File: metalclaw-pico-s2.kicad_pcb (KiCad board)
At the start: 4 copper layers, 21 x 51 mm, 73 parts, among them J1 USB_C_Receptacle_USB2.0_14P, J2 Conn_01x05, J3 Conn_02x05_Odd_Even, J4 Conn_Coaxial, SW1 SW_Push, SW2 SW_Push, U1 ESP32-S2, U2 MX25L3236FM2I-08G-TR, U3 APS6404L-3SQRx-SN, U5 XC6220B331MR, Y1 XRCGB40M000F1S2FR0

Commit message: Update PCB layout
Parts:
- removed D1: D_Schottky, Diode_SMD:D_SOD-323F
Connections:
- A2 pad 36: +3V3 -> unconnected-(A2-3V3-Pad36)
- A2 pad 39: VS -> unconnected-(A2-VSYS-Pad39)
- C1 pad 1: VS -> VBUS
- U5 pad 1: VS -> VBUS
- U5 pad 3: VS -> VBUS

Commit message: Fix non-board edge DRC errors
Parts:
- moved R4 4.64 mm to (158.0, 93.2), turned to 90 degrees
- moved R5 3.55 mm to (158.6, 91.2)
- moved R34 3.20 mm to (157.2, 87.0), turned to 90 degrees
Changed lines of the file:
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@@
 	(footprint "Resistor_SMD:R_0201_0603Metric"
 		(layer "F.Cu")
-		(at 158.86 89.7)
+		(at 157.15 87 90)
 		(descr "Resistor SMD 0201 (0603 Metric), square (rectangular) end terminal, IPC-7351 nominal, (Body size source: https://www.vishay.com/docs/20052/crcw0201e3.pdf), generated with kicad-footprint-generator")
 		(tags "resistor")
 		(property "Reference" "R34"
-			(at 0 -1.05 0)
+			(at 0 -1.05 90)
 			(layer "F.SilkS")
 			(effects
@@
 		)
 		(property "Value" "5.1k"
-			(at 0 1.05 0)
+			(at 0 1.05 90)
 			(layer "F.Fab")
 			(effects
@@
 		)
 		(property "Datasheet" "~"
-			(at 0 0 0)
+			(at 0 0 90)
 			(layer "F.Fab")
 			(hide yes)
@@
 		)
 		(property "Description" "Resistor, US symbol"
-			(at 0 0 0)
+			(at 0 0 90)
 			(layer "F.Fab")
 			(hide yes)
@@
 		)
 		(property "Mouser" "71-CRCW02015K10FEDAT "
-			(at 0 0 0)
+			(at 0 0 90)
 			(unlocked yes)
 			(layer "F.Fab")
@@
 		)
 		(fp_text user "${REFERENCE}"
-			(at 0 -0.68 0)
+			(at 0 -0.68 90)
 			(layer "F.Fab")
 			(effects
@@
 		)
 		(pad "" smd roundrect
-			(at -0.345 0)
+			(at -0.345 0 90)
 			(size 0.318 0.36)
 			(layers "F.Paste")
@@
 		)
 		(pad "" smd roundrect
-			(at 0.345 0)
+			(at 0.345 0 90)
 			(size 0.318 0.36)
 			(layers "F.Paste")
@@
 		)
 		(pad "1" smd roundrect
-			(at -0.32 0)
+			(at -0.32 0 90)
 			(size 0.46 0.4)
 			(layers "F.Cu" "F.Mask")
@@
 		)
 		(pad "2" smd roundrect
-			(at 0.32 0)
+			(at 0.32 0 90)
 			(size 0.46 0.4)
 			(layers "F.Cu" "F.Mask")
@@
 	(footprint "Resistor_SMD:R_0201_0603Metric"
 		(layer "F.Cu")
-		(at 161.09 88.75)
+		(at 158.55 91.23)
 		(descr "Resistor SMD 0201 (0603 Metric), square (rectangular) end terminal, IPC-7351 nominal, (Body size source: https://www.vishay.com/docs/20052/crcw0201e3.pdf), generated with kicad-footprint-generator")
 		(tags "resistor")
@@
 	(footprint "Resistor_SMD:R_0201_0603Metric"
 		(layer "F.Cu")
-		(at 158.67 88.61)
+		(at 158.03 93.21 90)
 		(descr "Resistor SMD 0201 (0603 Metric), square (rectangular) end terminal, IPC-7351 nominal, (Body size source: https://www.vishay.com/docs/20052/crcw0201e3.pdf), generated with kicad-footprint-generator")
 		(tags "resistor")
 		(property "Reference" "R4"
-			(at 0 -1.05 0)
+			(at 0 -1.05 90)
 			(layer "F.SilkS")
 			(effects
@@
 		)
 		(property "Value" "220"
-			(at 0 1.05 0)
+			(at 0 1.05 90)
 			(layer "F.Fab")
 			(effects
@@
 		)
 		(property "Datasheet" "~"
-			(at 0 0 0)
+			(at 0 0 90)
 			(layer "F.Fab")
 			(hide yes)
@@
 		)
 		(property "Description" "Resistor, US symbol"
-			(at 0 0 0)
+			(at 0 0 90)
 			(layer "F.Fab")
 			(hide yes)
@@
 		)
 		(property "Mouser" "603-AC0201FR-13220RL "
-			(at 0 0 0)
+			(at 0 0 90)
 			(unlocked yes)
 			(layer "F.Fab")
@@
 		)
 		(fp_text user "${REFERENCE}"
-			(at 0 -0.68 0)
+			(at 0 -0.68 90)
 			(layer "F.Fab")
 			(effects
@@
 		)
 		(pad "" smd roundrect
-			(at -0.345 0)
+			(at -0.345 0 90)
 			(size 0.318 0.36)
 			(layers "F.Paste")
@@
 		)
 		(pad "" smd roundrect
-			(at 0.345 0)
+			(at 0.345 0 90)
 			(size 0.318 0.36)
 			(layers "F.Paste")
@@
 		)
 		(pad "1" smd roundrect
-			(at -0.32 0)
+			(at -0.32 0 90)
 			(size 0.46 0.4)
 			(layers "F.Cu" "F.Mask")
@@
 		)
 		(pad "2" smd roundrect
-			(at 0.32 0)
+			(at 0.32 0 90)
 			(size 0.46 0.4)
 			(layers "F.Cu" "F.Mask")

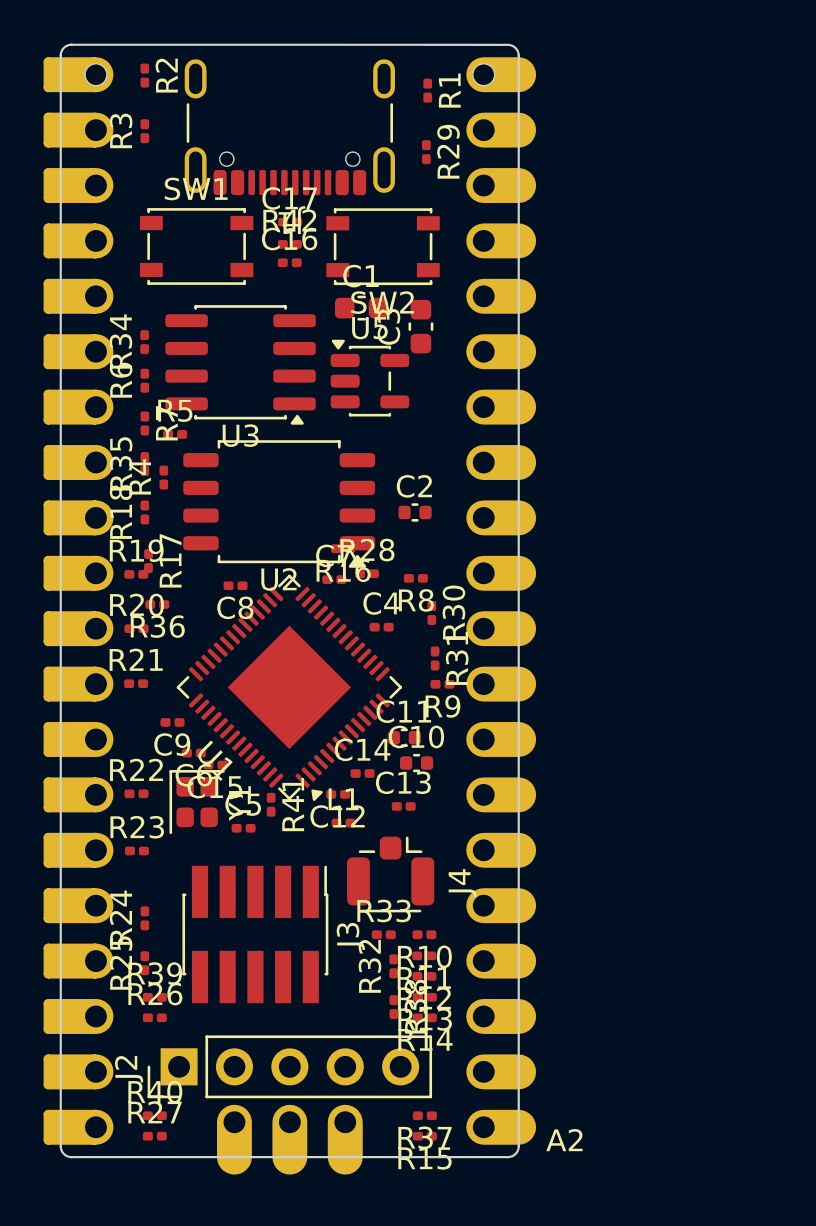
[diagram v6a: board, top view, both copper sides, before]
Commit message: Initial routing left side resistors
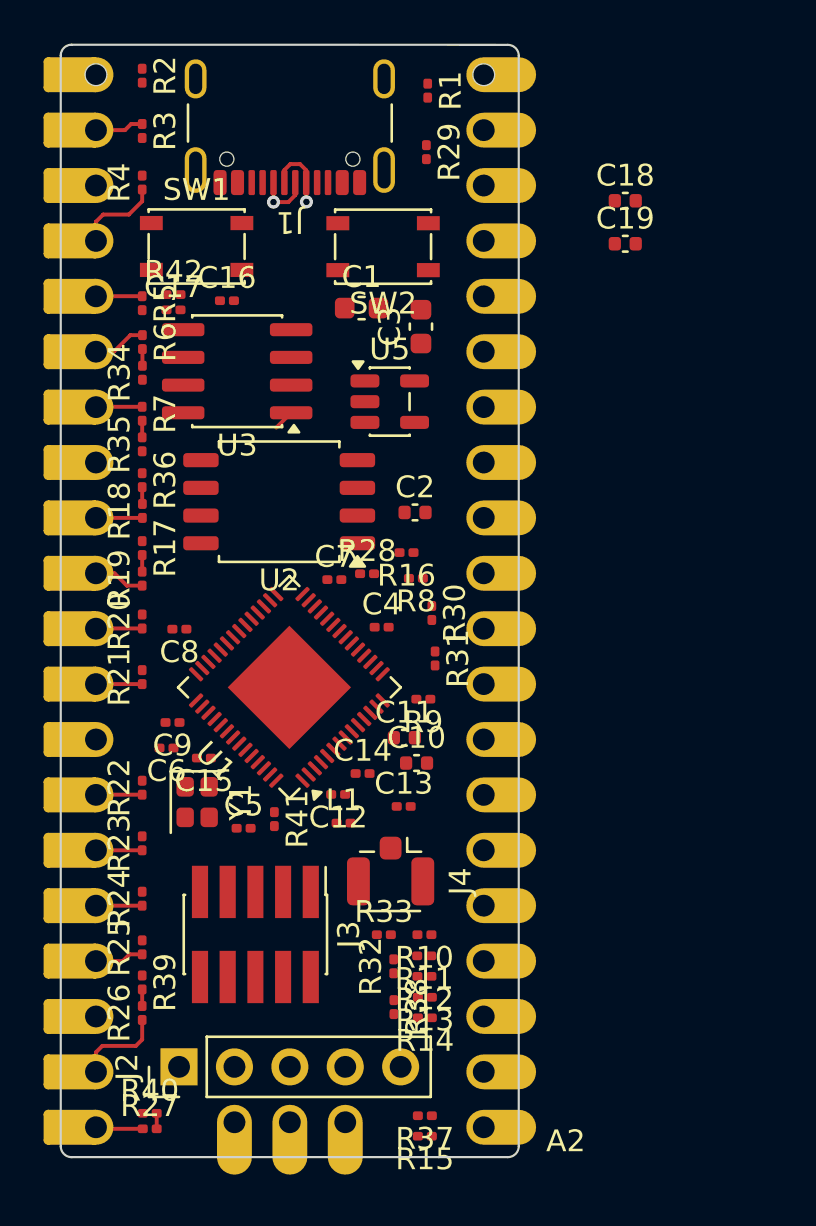
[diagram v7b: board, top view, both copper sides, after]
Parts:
- added C18: 1u, Capacitor_SMD:C_0402_1005Metric, F.Cu at (179.2, 80.5)
- added C19: 1u, Capacitor_SMD:C_0402_1005Metric, F.Cu at (179.2, 82.5)
- moved R4 13.6 mm to (157.0, 79.7)
- moved C17 6.69 mm to (158.5, 85.5)
- moved R5 6.20 mm to (157.0, 85.2), turned to -90 degrees
- moved R42 5.81 mm to (158.5, 84.8)
- moved R36 5.74 mm to (157.0, 93.3), turned to -90 degrees
- moved C16 3.36 mm to (160.9, 85.1)
- moved C8 3.25 mm to (158.7, 100.2)
- moved R16 2.92 mm to (169.2, 96.7)
- moved R6 1.77 mm to (157.1, 87.0), turned to -90 degrees
- moved R34 1.41 mm to (157.1, 88.4)
- moved U5 1.31 mm to (168.4, 89.7)
- moved C6 1.28 mm to (158.2, 105.6)
- moved R9 1.11 mm to (169.9, 103.4)
- moved R35 0.91 mm to (157.0, 91.7)
- moved R24 0.91 mm to (157.0, 112.5)
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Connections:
- net Net-(U1-GPIO19/USB_D-) renamed /USB_D-
- net Net-(U1-GPIO20/USB_D+) renamed /USB_D+
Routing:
- net Net-(A2-GPIO14): track 0.00 -> 4.16 mm
- net Net-(A2-GPIO2): track 0.00 -> 3.92 mm
- net /USB_D-: track 0.00 -> 3.26 mm, vias 0 -> 1
- net Net-(A2-GPIO1): track 0.00 -> 2.63 mm
- net /USB_D+: track 0.00 -> 2.60 mm, vias 0 -> 1
- net Net-(A2-GPIO4): track 0.00 -> 2.44 mm
- net Net-(A2-GPIO7): track 0.00 -> 2.35 mm
- net Net-(A2-GPIO13): track 0.00 -> 2.26 mm
- net Net-(A2-GPIO15): track 0.00 -> 2.17 mm
- net Net-(A2-GPIO6): track 0.00 -> 2.13 mm
- net Net-(A2-GPIO5): track 0.00 -> 2.13 mm
- net Net-(A2-GPIO8): track 0.00 -> 2.12 mm
- net Net-(A2-GPIO10): track 0.00 -> 2.12 mm
- net Net-(A2-GPIO3): track 0.00 -> 2.12 mm
- net Net-(A2-GPIO9): track 0.00 -> 2.12 mm
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
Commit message: Change I2C pins
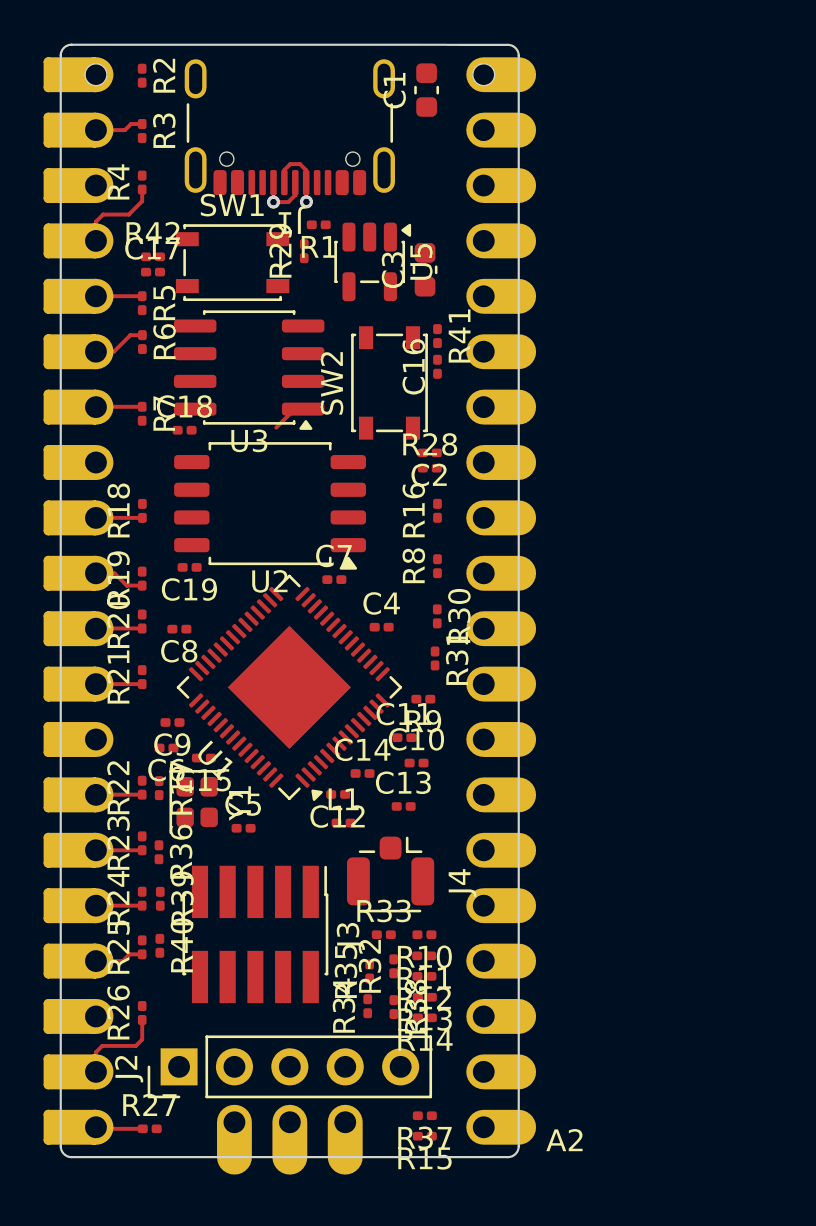
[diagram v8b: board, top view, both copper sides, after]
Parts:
- C10, C11, C18, C19, C2: footprint Capacitor_SMD:C_0402_1005Metric -> Capacitor_SMD:C_0201_0603Metric
- moved R34 30.8 mm to (167.4, 117.5)
- moved R35 26.3 mm to (167.5, 115.9)
- moved C19 24.9 mm to (159.2, 97.3), turned to 180 degrees
- moved R41 23.4 mm to (170.6, 86.7)
- moved C18 22.8 mm to (159.0, 91.0)
- moved R36 17.1 mm to (157.8, 110.4)
- moved R17 11.0 mm to (157.8, 107.5)
- moved C1 10.4 mm to (170.1, 75.4), turned to 90 degrees
- moved C16 10.1 mm to (170.6, 88.1), turned to 90 degrees
- moved R1 7.92 mm to (165.1, 81.6), turned to 180 degrees
- moved R40 7.69 mm to (157.8, 114.7), turned to -90 degrees
- moved R29 7.21 mm to (164.5, 82.8), turned to 90 degrees
- moved U5 6.47 mm to (167.5, 83.3), turned to -90 degrees
- moved SW2 6.25 mm to (168.4, 88.9), turned to 90 degrees
- moved R28 5.63 mm to (170.2, 92.8)
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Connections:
- R17 pad 2: /GP7 -> /GP10
- R34 pad 2: /GP4 -> /GP19
- R35 pad 2: /GP5 -> /GP18
- R36 pad 2: /GP6 -> /GP11
- R39 pad 2: /GP14 -> /GP12
- R40 pad 2: /GP15 -> /GP13
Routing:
- net /GP4: track 0.77 -> 0.00 mm
- net /GP7: track 0.76 -> 0.00 mm
- net /GP6: track 0.77 -> 0.01 mm
- net /GP5: track 0.76 -> 0.00 mm
- net /GP14: track 0.76 -> 0.00 mm
- net /GP15: track 0.71 -> 0.00 mm
